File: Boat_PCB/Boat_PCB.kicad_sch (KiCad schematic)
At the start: 44 parts, among them J1 Conn_02x06_Odd_Even, J10 IMU, J11 Temp + Humidity Sensor, J12 led, J13 Temp + Humidity Sensor, J14 Conn_01x20_Socket, J15 Hull Leak 20, J16 Hull Leak 19, J17 Conn_01x20_Socket, J2 CAN chain, J3 Raspberry Pi 5 connector, J4 12s output, J5 12s output, J6 6s output, J7 GPS + Compass, J8 Winch ESC, J9 Winch ESC RC

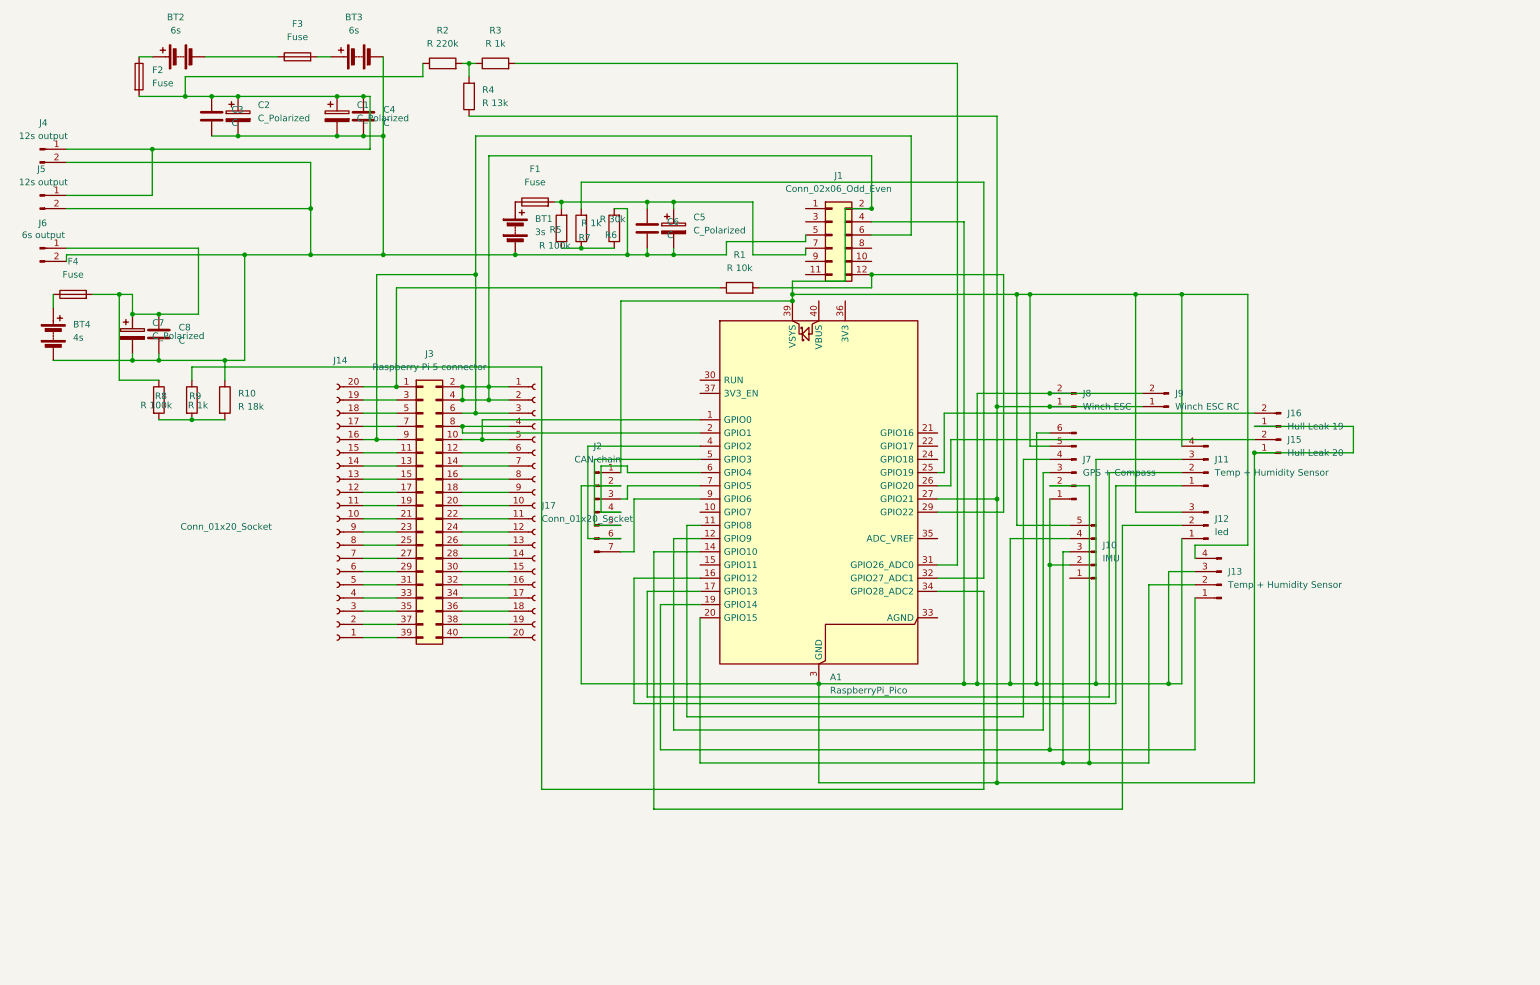
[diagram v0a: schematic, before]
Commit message: Align-first steering, waypoint planner page, and M18 battery migration
Replaces proximity-boost turn logic with an align-first controller that
pivots the boat to face the next waypoint before driving forward, fixing
orbiting around waypoints. Adds a standalone waypoint planner page with a
saved-path library, wired into the command center's LOAD PATH picker and
SET HDG control. Also carries forward the three-domain Milwaukee M18
battery migration in firmware/docs and the KiCad schematic/PCB rework to
match the new divider values.

Co-Authored-By: Claude Sonnet 5 <noreply@anthropic.com>
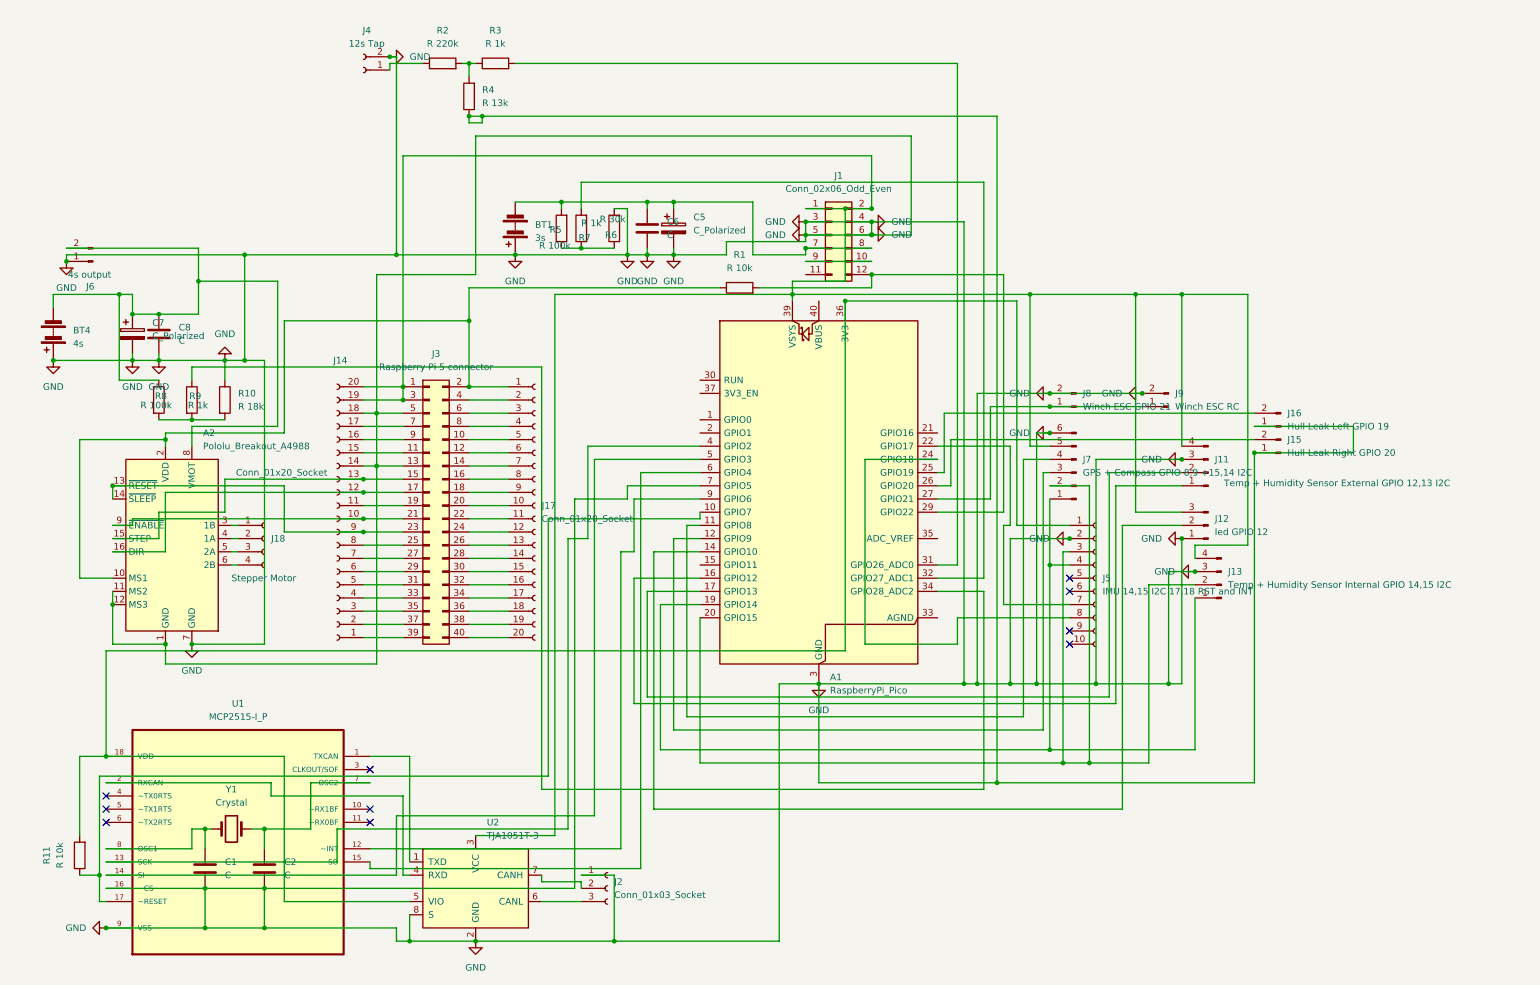
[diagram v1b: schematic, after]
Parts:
- removed BT2, BT3: 6s, Connector_AMASS:AMASS_XT60-M_1x02_P7.20mm_Vertical, symbol Device:Battery
- removed C1, C2: C_Polarized, Capacitor_THT:CP_Radial_D10.0mm_P5.00mm, symbol Device:C_Polarized
- removed C3, C4: C, Capacitor_THT:C_Disc_D5.0mm_W2.5mm_P5.00mm, symbol Device:C
- removed F1: Fuse, Fuse:Fuse_Blade_ATO_directSolder, symbol Device:Fuse
- removed F2, F3, F4: Fuse, symbol Device:Fuse
- removed J10: IMU, Connector_PinHeader_2.54mm:PinHeader_1x05_P2.54mm_Vertical, symbol Connector:Conn_01x05_Pin
- removed J2: CAN chain, Connector_PinHeader_2.54mm:PinHeader_1x07_P2.54mm_Vertical, symbol Connector:Conn_01x07_Pin
- removed J4, J5: 12s output, Connector_AMASS:AMASS_XT90PW-M_1x02_P10.90mm_Horizontal, symbol Connector:Conn_01x02_Pin
- added A2: Pololu_Breakout_A4988, Module:Pololu_Breakout-16_15.2x20.3mm, symbol Driver_Motor:Pololu_Breakout_A4988
- added C1, C2: C, Capacitor_THT:C_Disc_D3.0mm_W1.6mm_P2.50mm, symbol Device:C
- added J18: Stepper Motor, Connector_JST:JST_XH_B4B-XH-A_1x04_P2.50mm_Vertical, symbol Connector:Conn_01x04_Socket
- added J2: Conn_01x03_Socket, Connector_JST:JST_XH_B3B-XH-A_1x03_P2.50mm_Vertical, symbol Connector:Conn_01x03_Socket
- added J4: 12s Tap, Connector_JST:JST_XH_B2B-XH-A_1x02_P2.50mm_Vertical, symbol Connector:Conn_01x02_Socket
- added J5: IMU 14,15 I2C 17,18 RST and INT., Connector_JST:JST_XH_B10B-XH-A_1x10_P2.50mm_Vertical, symbol Connector:Conn_01x10_Socket
- added R11: R 10k, Resistor_THT:R_Axial_DIN0207_L6.3mm_D2.5mm_P10.16mm_Horizontal, symbol Device:R
- added U1: MCP2515-I_P, MCP2515-I_P:DIP254P762X432-18, symbol MCP2515-I_P:MCP2515-I_P
- added U2: TJA1051T-3, Package_SO:SOIC-8_3.9x4.9mm_P1.27mm, symbol Interface_CAN_LIN:TJA1051T-3
- added Y1: Crystal, Crystal:Crystal_HC49-4H_Vertical, symbol Device:Crystal
- A1: footprint Module:RaspberryPi_Pico_Common_Unspecified -> Module:Raspberry pico no antenna
- BT4: footprint Connector_AMASS:AMASS_XT30PW-M_1x02_P2.50mm_Horizontal -> Connector_AMASS:AMASS_XT60-M_1x02_P7.20mm_Vertical
- J1: footprint Connector_PinHeader_2.54mm:PinHeader_2x06_P2.54mm_Vertical -> Module:Pololu 36v5vstepdown
- J11: value Temp + Humidity Sensor -> Temp + Humidity Sensor External GPIO 12,13 I2C; footprint Connector_PinHeader_2.54mm:PinHeader_1x04_P2.54mm_Vertical -> Connector_JST:JST_XH_B4B-XH-A_1x04_P2.50mm_Vertical
- J12: value led -> led GPIO 12
- J13: value Temp + Humidity Sensor -> Temp + Humidity Sensor Internal GPIO 14,15 I2C
- J14, J17: footprint Connector_PinHeader_2.54mm:PinHeader_1x20_P2.54mm_Vertical -> Connector_PinSocket_2.54mm:PinSocket_1x20_P2.54mm_Vertical
- J15: value Hull Leak 20 -> Hull Leak Right GPIO 20
- J16: value Hull Leak 19 -> Hull Leak Left GPIO 19
- J3: footprint Connector_PinHeader_2.54mm:PinHeader_2x20_P2.54mm_Vertical -> Module:Raspberry Pi Mounting
- J6: value 6s output -> 4s output; footprint Connector_AMASS:AMASS_XT60IPW-M_1x03_P7.20mm_Horizontal -> Connector_AMASS:AMASS_XT60-M_1x02_P7.20mm_Vertical
- J7: value GPS + Compass -> GPS + Compass GPIO 8,9 +15,14 I2C; footprint Connector_JST:JST_SH_SM06B-SRSS-TB_1x06-1MP_P1.00mm_Horizontal -> Connector_JST:JST_XH_B6B-XH-A_1x06_P2.50mm_Vertical
- J8: value Winch ESC -> Winch ESC GPIO 21; footprint Connector_JST:JST_XH_S2B-XH-A_1x02_P2.50mm_Horizontal -> Connector_JST:JST_XH_B2B-XH-A_1x02_P2.50mm_Vertical
- J9: footprint Connector_PinHeader_2.54mm:PinHeader_1x02_P2.54mm_Vertical -> Connector_PinSocket_2.54mm:PinSocket_1x02_P2.54mm_Vertical
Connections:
- net GND: now reaches C5.2, C6.2, C7.2, C8.2, J1.5 (Pin_5), R10.1, R6.2
- net GND: now also A1.13 (GND), A1.18 (GND), A1.23 (GND), A1.28 (GND), A1.3 (GND), A1.38 (GND), A1.7 (GPIO5), A1.8 (GND), BT1.1 (+), BT4.1 (+), J1.3 (Pin_3), J1.4 (Pin_4), J1.6 (Pin_6), J11.3 (Pin_3), J12.1 (Pin_1), J13.3 (Pin_3), J14.14 (Pin_14), J14.18 (Pin_18), J15.1 (Pin_1), J16.1 (Pin_1), J3.13 (Pin_13), J3.5 (Pin_5), J6.1 (Pin_1), J7.6 (Pin_6), J8.2 (Pin_2), J9.2 (Pin_2), R4.1, A2.1 (GND), A2.11 (MS2), A2.12 (MS3), A2.7 (GND), C1.1, C2.1, J2.1 (Pin_1), J4.2 (Pin_2), J5.2 (Pin_2), U1.16 (~CS), U1.9 (VSS), U2.2 (GND), U2.8 (S); no longer BT1.2 (-), BT4.2 (-), J6.2 (Pin_2)
- net at C7.1, C8.1, R8.1: now also BT4.2 (-), J6.2 (Pin_2), A2.8 (VMOT); no longer J6.1 (Pin_1)
- net at R2.1: now also J4.1 (Pin_1)
- net at J17.5 (Pin_5), J3.10 (Pin_10): no longer A1.1 (GPIO0)
- net at A1.10 (GPIO7): now also R11.1, U1.17 (~RESET)
- net at A1.19 (GPIO14), J13.1 (Pin_1), J7.1 (Pin_1): now also J5.4 (Pin_4)
- net at J17.4 (Pin_4), J3.8 (Pin_8): no longer A1.2 (GPIO1)
- net at A1.20 (GPIO15), J13.2 (Pin_2), J7.2 (Pin_2): now also J5.3 (Pin_3)
- net at A1.22 (GPIO17): now also J5.7 (Pin_7)
- net at A1.24 (GPIO18): now also J5.8 (Pin_8)
- net at A1.36 (3V3): now also J5.1 (Pin_1), R11.2, U1.18 (VDD), U2.5 (VIO)
- net at A1.39 (VSYS), J1.2 (Pin_2), J11.4 (Pin_4)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: now also J1.1 (Pin_1), J14.19 (Pin_19), J14.20 (Pin_20), J3.1 (Pin_1), J3.3 (Pin_3), U2.3 (VCC); no longer J17.1 (Pin_1), J17.2 (Pin_2), J3.2 (Pin_2), J3.4 (Pin_4)
- net at A1.4 (GPIO2): now also U1.13 (SCK)
- net at A1.5 (GPIO3): now also U1.14 (SI)
- net at A1.6 (GPIO4): now also U1.15 (SO)
- net at A1.9 (GPIO6): now also U1.12 (~INT)
- net at J1.10 (Pin_10): now also J1.9 (Pin_9)
- net at C5.1, C6.1, J1.7 (Pin_7)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: now also BT1.2 (-), J1.8 (Pin_8)
- net at J14.10 (Pin_10), J3.21 (Pin_21): now also A2.9 (~{ENABLE})
- net at J14.12 (Pin_12), J3.17 (Pin_17): now also A2.16 (DIR)
- net at J14.13 (Pin_13), J3.15 (Pin_15): now also A2.15 (STEP)
- net at J14.9 (Pin_9), J3.23 (Pin_23): now also A2.13 (~{RESET}), A2.14 (~{SLEEP})
- new net: J2.2 (Pin_2), U2.7 (CANH)
- new net: J2.3 (Pin_3), U2.6 (CANL)
- new net: A1.27 (GPIO21), J8.1 (Pin_1), J9.1 (Pin_1)
- new net: A2.10 (MS1), A2.2 (VDD), J17.1 (Pin_1), J3.2 (Pin_2), R1.1
- new net: A2.3 (1B), J18.1 (Pin_1)
- new net: A2.4 (1A), J18.2 (Pin_2)
- new net: A2.5 (2A), J18.3 (Pin_3)
- new net: A2.6 (2B), J18.4 (Pin_4)
- new net: C1.2, U1.8 (OSC1), Y1.1
- new net: C2.2, U1.7 (OSC2), Y1.2
- new net: U1.1 (TXCAN), U2.1 (TXD)
- new net: U1.2 (RXCAN), U2.4 (RXD)
- new net: J14.16 (Pin_16), J3.9 (Pin_9)
- new net: J17.2 (Pin_2), J3.4 (Pin_4)
- new net: J17.3 (Pin_3), J3.6 (Pin_6)
- no-connect marks 0 -> 10
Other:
- moved on the sheet: BT1, BT4, J3, J6
